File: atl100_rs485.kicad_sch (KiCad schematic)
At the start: 1 part, among them U3 HW-519

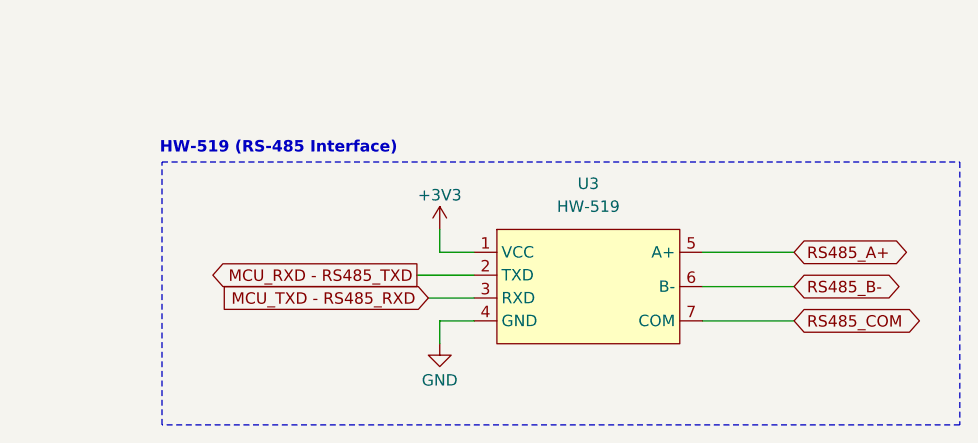
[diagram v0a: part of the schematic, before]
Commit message: feat: Main board schematic updated
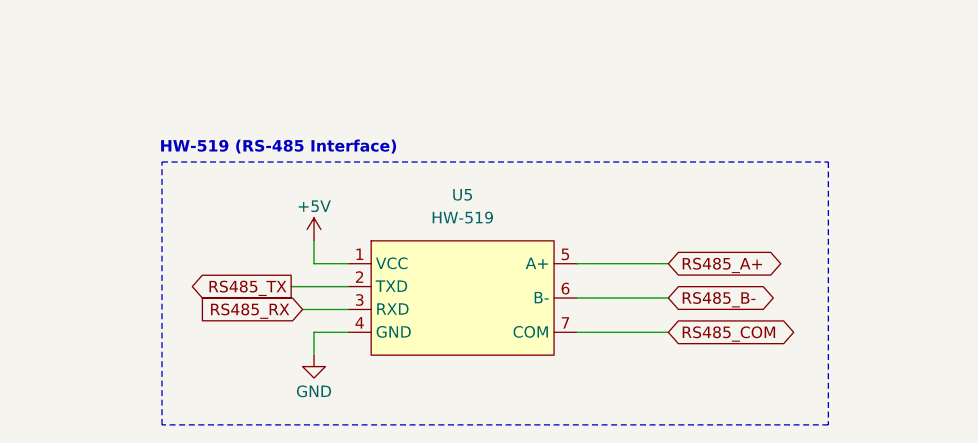
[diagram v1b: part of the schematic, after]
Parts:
- renumbered U3 to U5
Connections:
- net +3V3 renamed +5V
- net MCU_RXD - RS485_TXD renamed RS485_TX
- net MCU_TXD - RS485_RXD renamed RS485_RX
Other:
- title: ATL-100 (Multiparametric Station) -> ATL-100 (Multiparametric Station) - Main Board
- moved on the sheet: U5
